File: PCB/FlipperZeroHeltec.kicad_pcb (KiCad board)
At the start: 2 copper layers, 65 x 30 mm, 2 parts, among them U1 WIFI_KIT_32__V3_

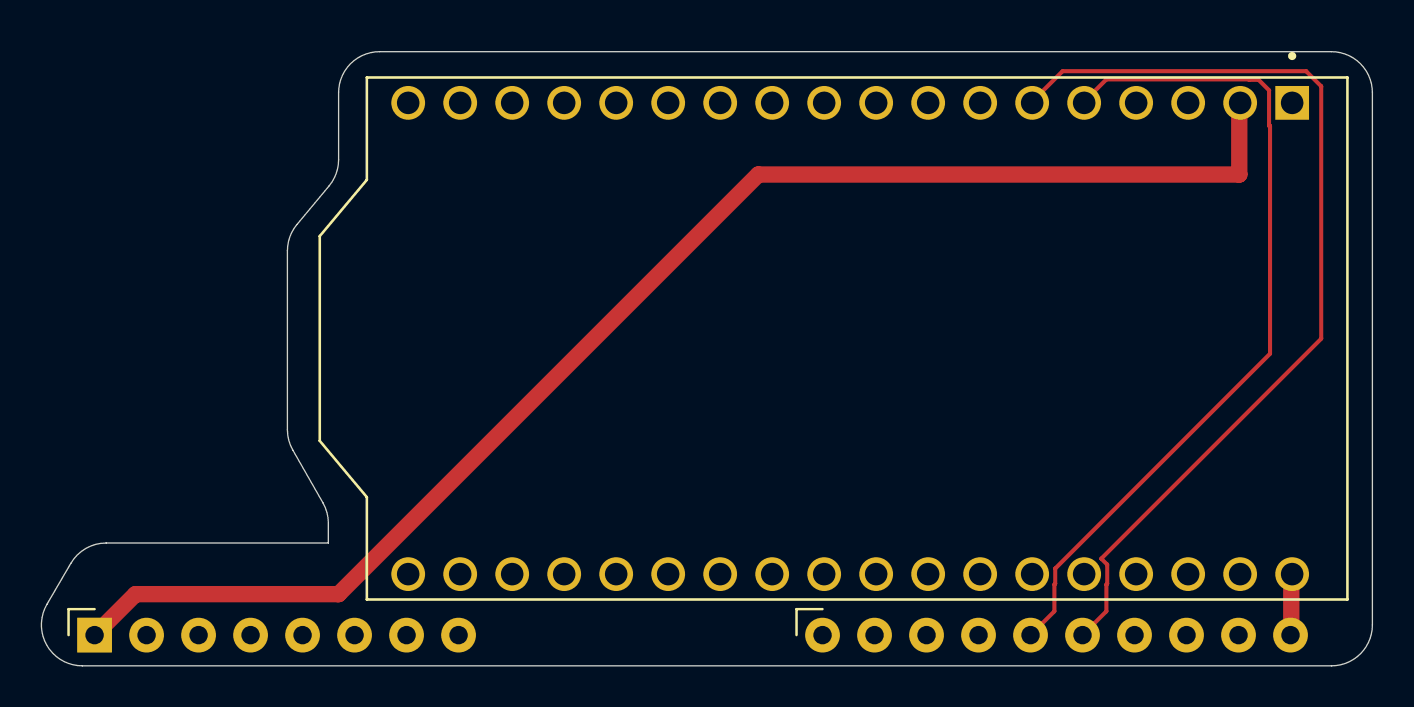
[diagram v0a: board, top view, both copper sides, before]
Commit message: Further refinements on geometry and adding text
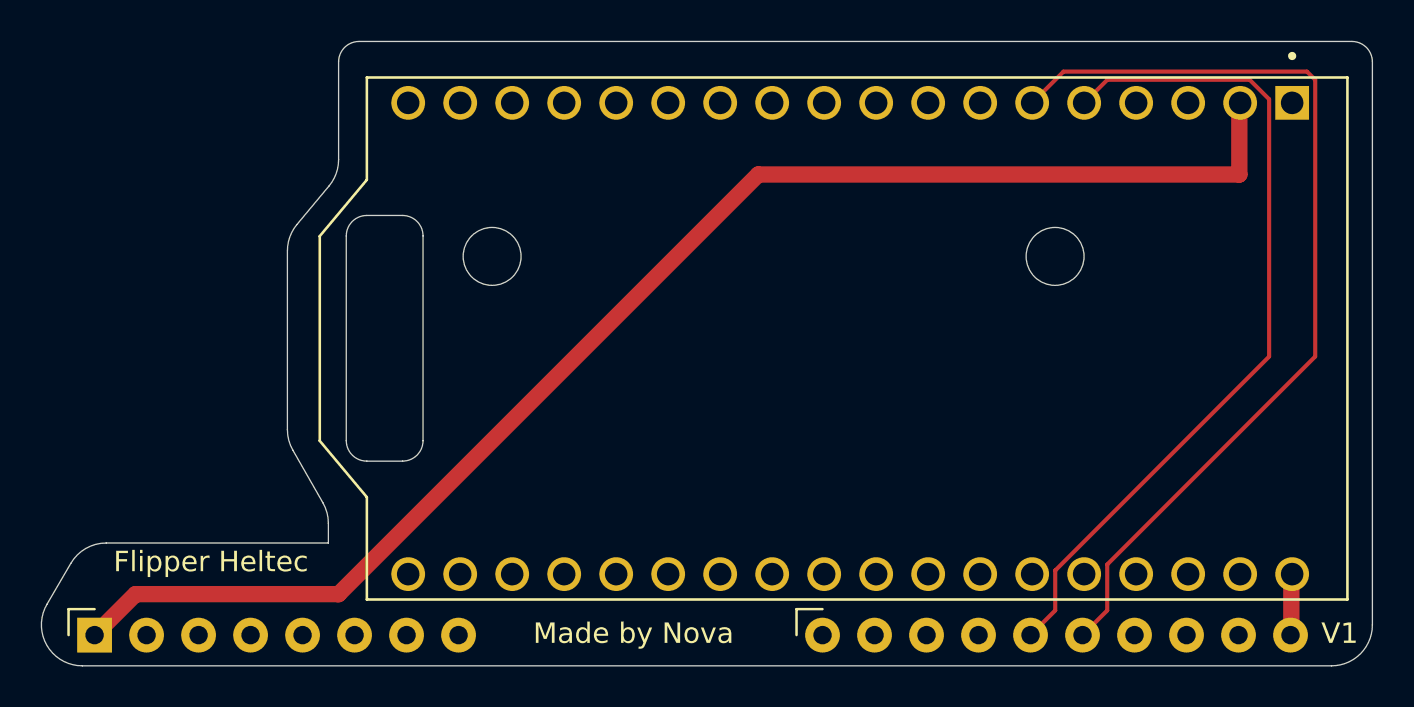
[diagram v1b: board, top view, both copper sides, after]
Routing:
- net Net-(A1-USART1.RX): track 47.0 -> 46.5 mm
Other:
- board size 65 x 30 mm -> 65 x 30.5 mm
- board text added: "Flipper Heltec"
- board text added: "Made by Nova"
- board text added: "V1"
